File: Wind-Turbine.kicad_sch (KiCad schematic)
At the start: 17 parts, among them U1 INA101HP

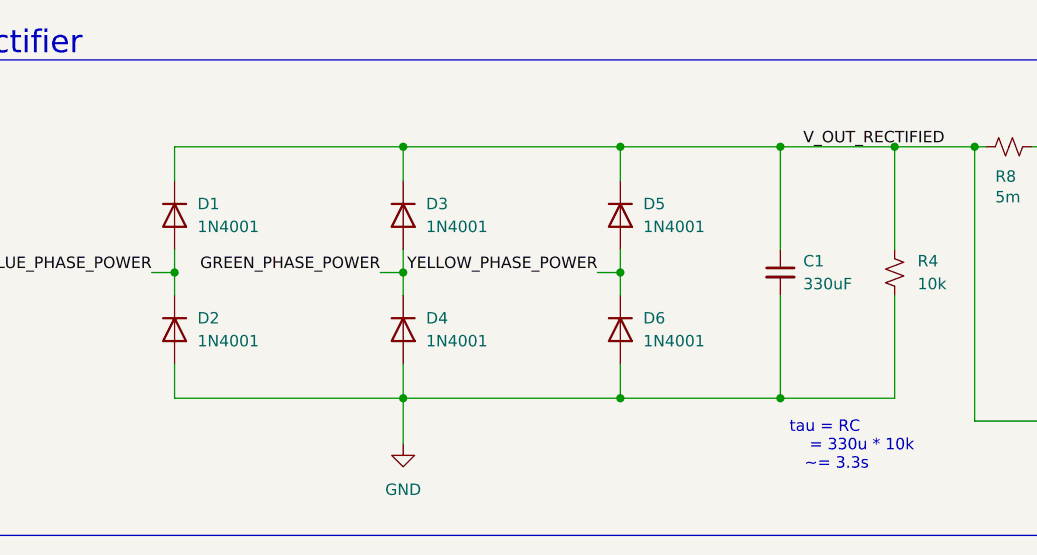
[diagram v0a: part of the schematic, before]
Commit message: Update rectifier components for high power
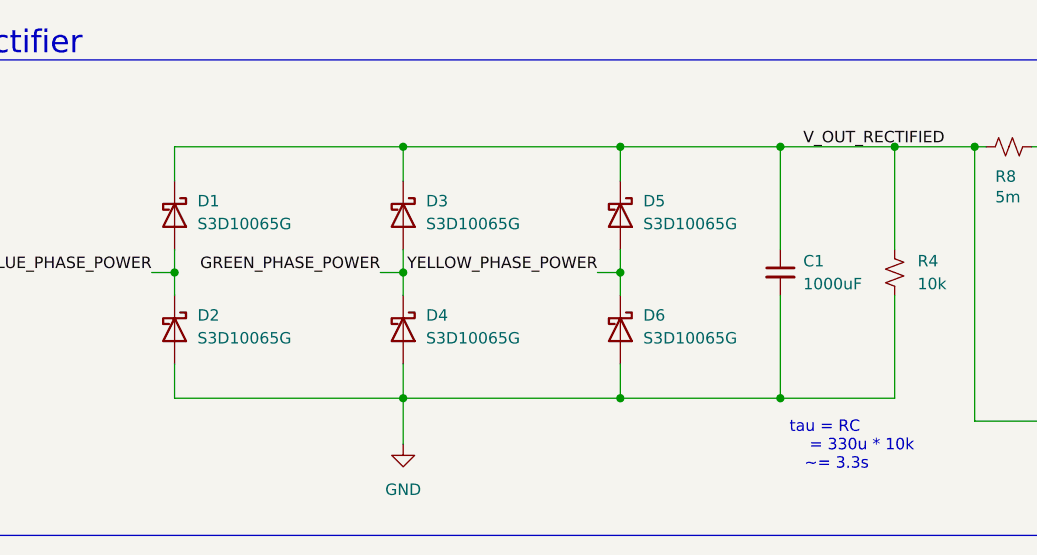
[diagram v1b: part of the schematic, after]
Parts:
- removed D1, D2, D3, D4, D5, D6: 1N4001, Diode_THT:D_DO-41_SOD81_P10.16mm_Horizontal, symbol Diode:1N4001
- added D1, D2, D3, D4, D5, D6: S3D10065G, Package_TO_SOT_SMD:TO-263-2_TabPin1, symbol Device:D_Schottky
- C1: value 330uF -> 1000uF; footprint (none) -> Capacitor_THT:CP_Radial_D25.0mm_P10.00mm_SnapIn
- R4: footprint (none) -> Resistor_SMD:R_2512_6332Metric_Pad1.40x3.35mm_HandSolder
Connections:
- net BLUE_PHASE_POWER: now also D1.2 (A), D2.1 (K)
- net GND: now also D2.2 (A), D4.2 (A), D6.2 (A)
- net GREEN_PHASE_POWER: now also D3.2 (A), D4.1 (K)
- net V_OUT_RECTIFIED: now also D1.1 (K), D3.1 (K), D5.1 (K)
- net YELLOW_PHASE_POWER: now also D5.2 (A), D6.1 (K)
